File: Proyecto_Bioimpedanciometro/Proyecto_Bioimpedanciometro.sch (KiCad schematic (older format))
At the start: 29 parts, among them IC1 ATMEGA328P-A, P1 CONN_01X09, P2 CONN_01X03, P3 CONN_01X04, U1 ADG849, U2 AD8606, U3 APD3339, Y1 Crystal_Small

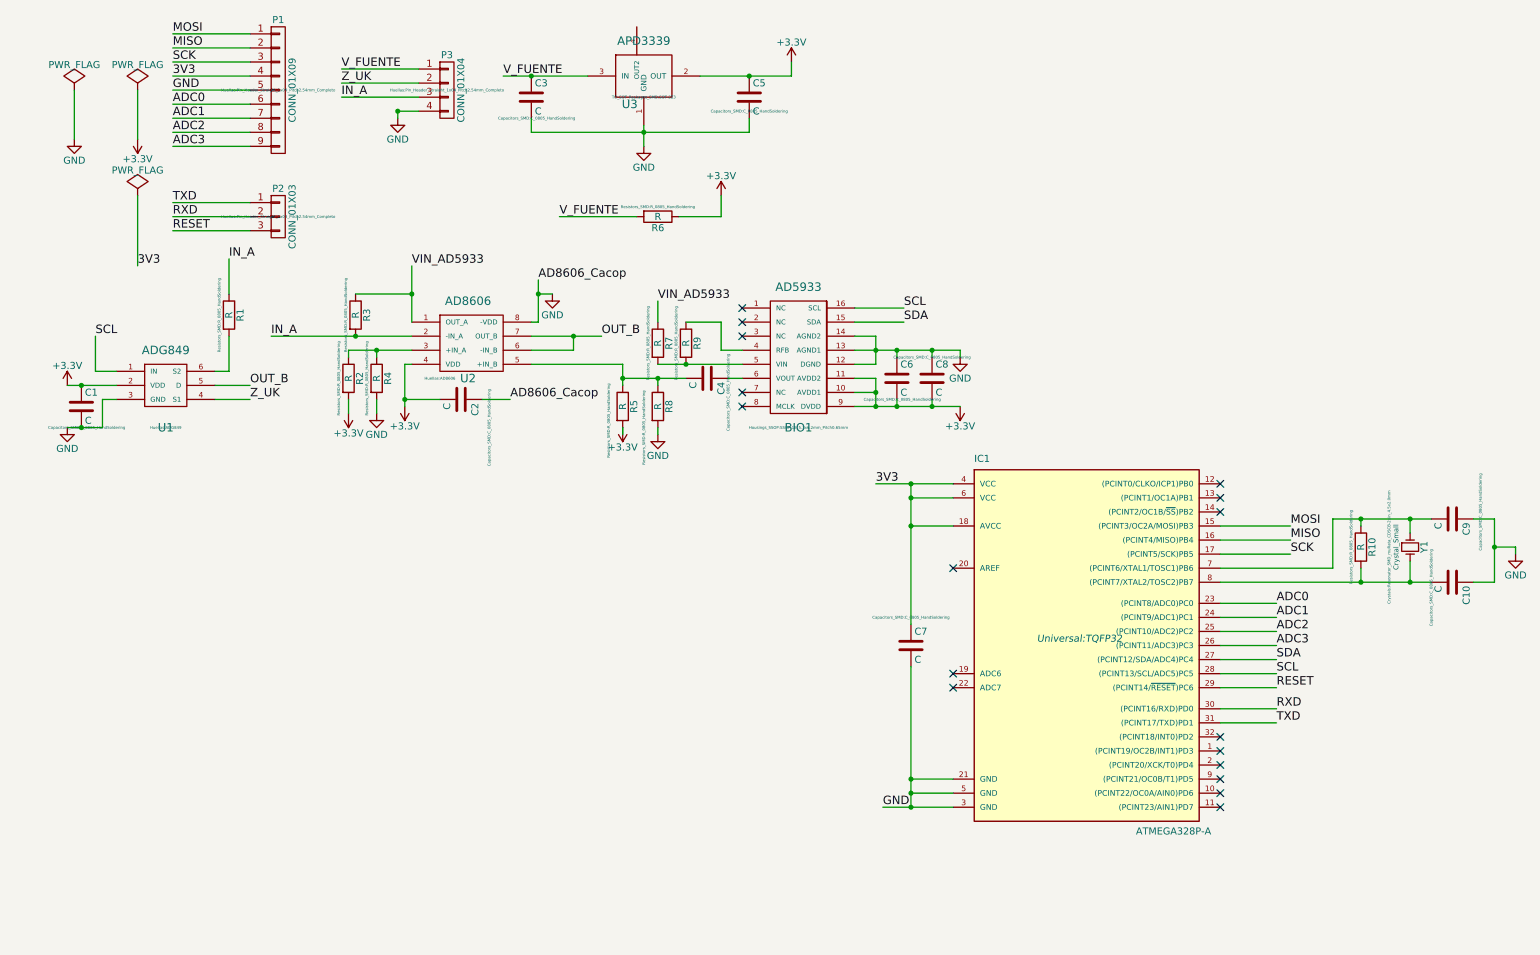
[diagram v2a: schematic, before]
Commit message: Cuarta Versión
Revisar todo el diseño y errores mas importantes
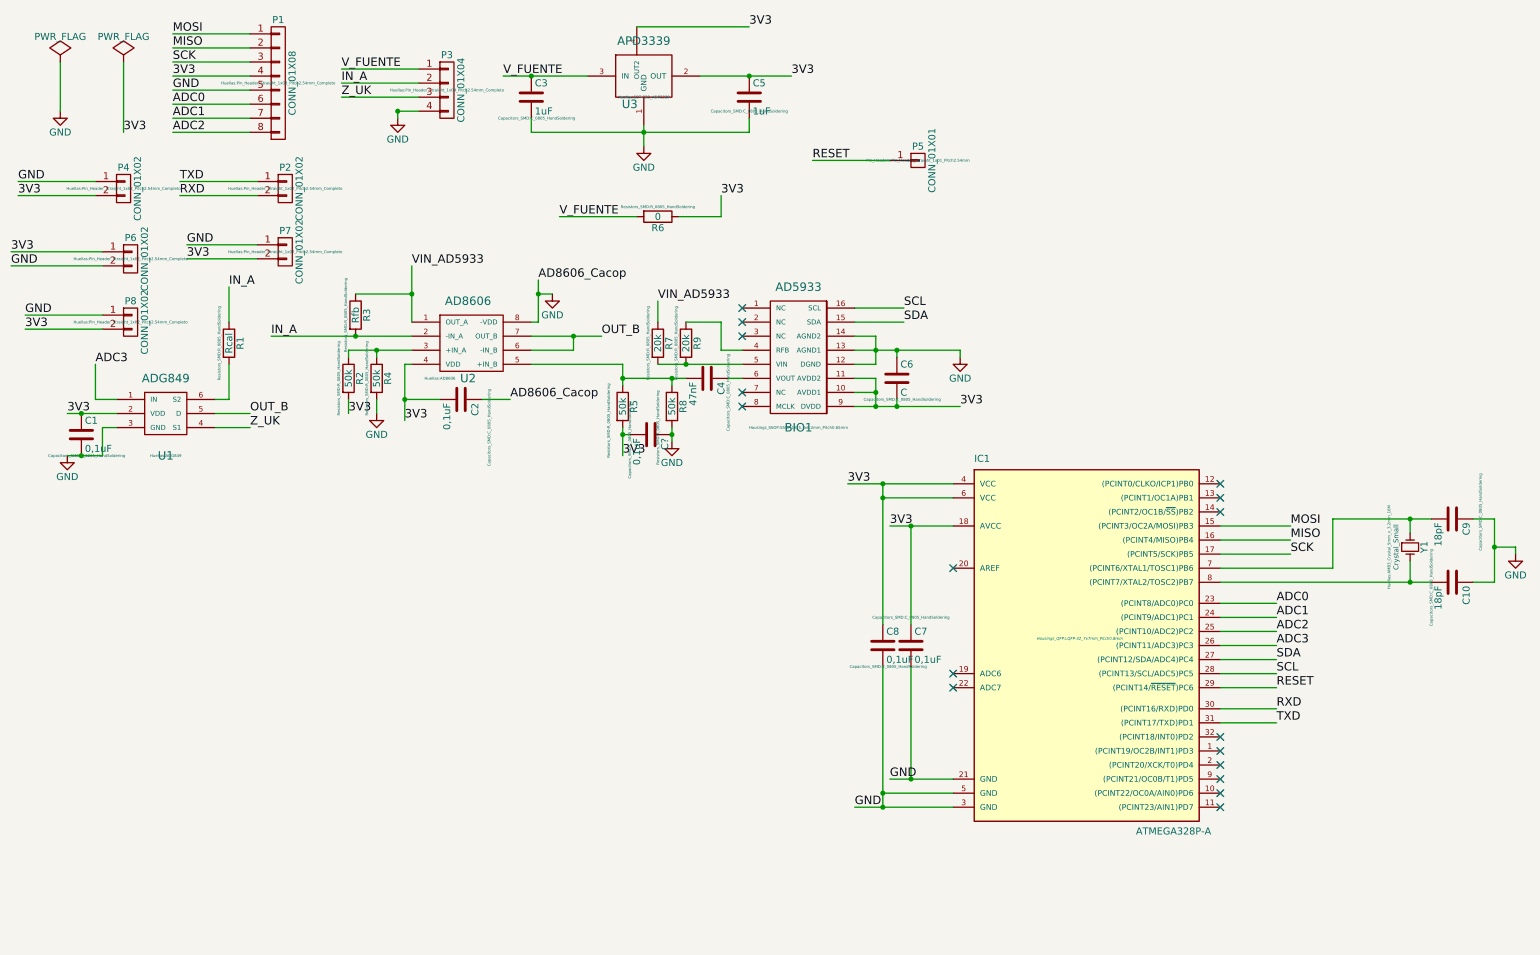
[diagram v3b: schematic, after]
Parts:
- removed P1: CONN_01X09, Huellas:Pin_Header_Straight_1x09_Pitch2.54mm_Completo, symbol CONN_01X09
- removed P2: CONN_01X03, Huellas:Pin_Header_Straight_1x03_Pitch2.54mm_Completo, symbol CONN_01X03
- removed R10: R, Resistors_SMD:R_0805_HandSoldering, symbol R
- added C?: 0,1uF, Capacitors_SMD:C_0805_HandSoldering, symbol C
- added P1: CONN_01X08, Huellas:Pin_Header_Straight_1x08_Pitch2.54mm_Completo, symbol CONN_01X08
- added P2, P4, P6, P7, P8: CONN_01X02, Huellas:Pin_Header_Straight_1x02_Pitch2.54mm_Completo, symbol CONN_01X02
- added P5: CONN_01X01, Pin_Headers:Pin_Header_Straight_1x01_Pitch2.54mm, symbol CONN_01X01
- C1, C2, C7, C8: value C -> 0,1uF
- C10, C9: value C -> 18pF
- C3, C5: value C -> 1uF
- C4: value C -> 47nF
- IC1: footprint Universal:TQFP32 -> Housings_QFP:LQFP-32_7x7mm_Pitch0.8mm
- R1: value R -> Rcal
- R2, R4, R5, R8: value R -> 50k
- R3: value R -> Rfb
- R6: value R -> 0
- R7, R9: value R -> 20k
- U3: footprint TO_SOT_Packages_SMD:SOT-223 -> Huellas:SOT-223_ADP3339
- Y1: footprint Crystals:Resonator_SMD_muRata_CDSCB-2pin_4.5x2.0mm -> Huellas:AMB3_Crystal_5mm_x_3,2mm_16M
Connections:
- net 3V3: now also BIO1.10 (AVDD1), BIO1.11 (AVDD2), BIO1.9 (DVDD), C1.1, C2.2, C5.1, C6.2, C8.1, R2.2, R5.2, R6.1, U1.2 (VDD), U2.4 (VDD), U3.2 (OUT), U3.4 (OUT2), C?.2, P1.4 (P4), P4.2 (P2), P6.1 (P1), P7.2 (P2), P8.2 (P2)
- net ADC0: now also P1.6 (P6)
- net ADC1: now also P1.7 (P7)
- net ADC2: now also P1.8 (P8)
- net ADC3: now also U1.1 (IN)
- net GND: now also C8.2, C?.1, P1.5 (P5), P4.1 (P1), P6.2 (P2), P7.1 (P1), P8.1 (P1); no longer C8.1
- net IN_A: now also P3.2 (P2); no longer P3.3 (P3)
- net MISO: now also P1.2 (P2)
- net MOSI: now also P1.1 (P1)
- net RESET: now also P5.1 (P1)
- net RXD: now also P2.2 (P2)
- net SCK: now also P1.3 (P3)
- net SCL: no longer U1.1 (IN)
- net TXD: now also P2.1 (P1)
- net Z_UK: now also P3.3 (P3); no longer P3.2 (P2)
- removed net +3V3: BIO1.10 (AVDD1), BIO1.11 (AVDD2), BIO1.9 (DVDD), C1.1, C2.2, C5.1, C6.2, C8.2, R2.2, R5.2, R6.1, U1.2 (VDD), U2.4 (VDD), U3.2 (OUT)
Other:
- moved on the sheet: C1, R1, R8, U1

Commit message: Diseño a corregir
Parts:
- gave numbers to parts that had none: 1
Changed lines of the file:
@@
 Connection ~ 5150 3100
 $Comp
-L C C?
+L C C11
 U 1 1 59133D08
 P 5000 3500
-F 0 "C?" H 5025 3600 50  0000 L CNN
+F 0 "C11" H 5025 3600 50  0000 L CNN
 F 1 "0,1uF" H 5025 3400 50  0000 L CNN
 F 2 "Capacitors_SMD:C_0805_HandSoldering" H 5038 3350 20  0000 C CNN

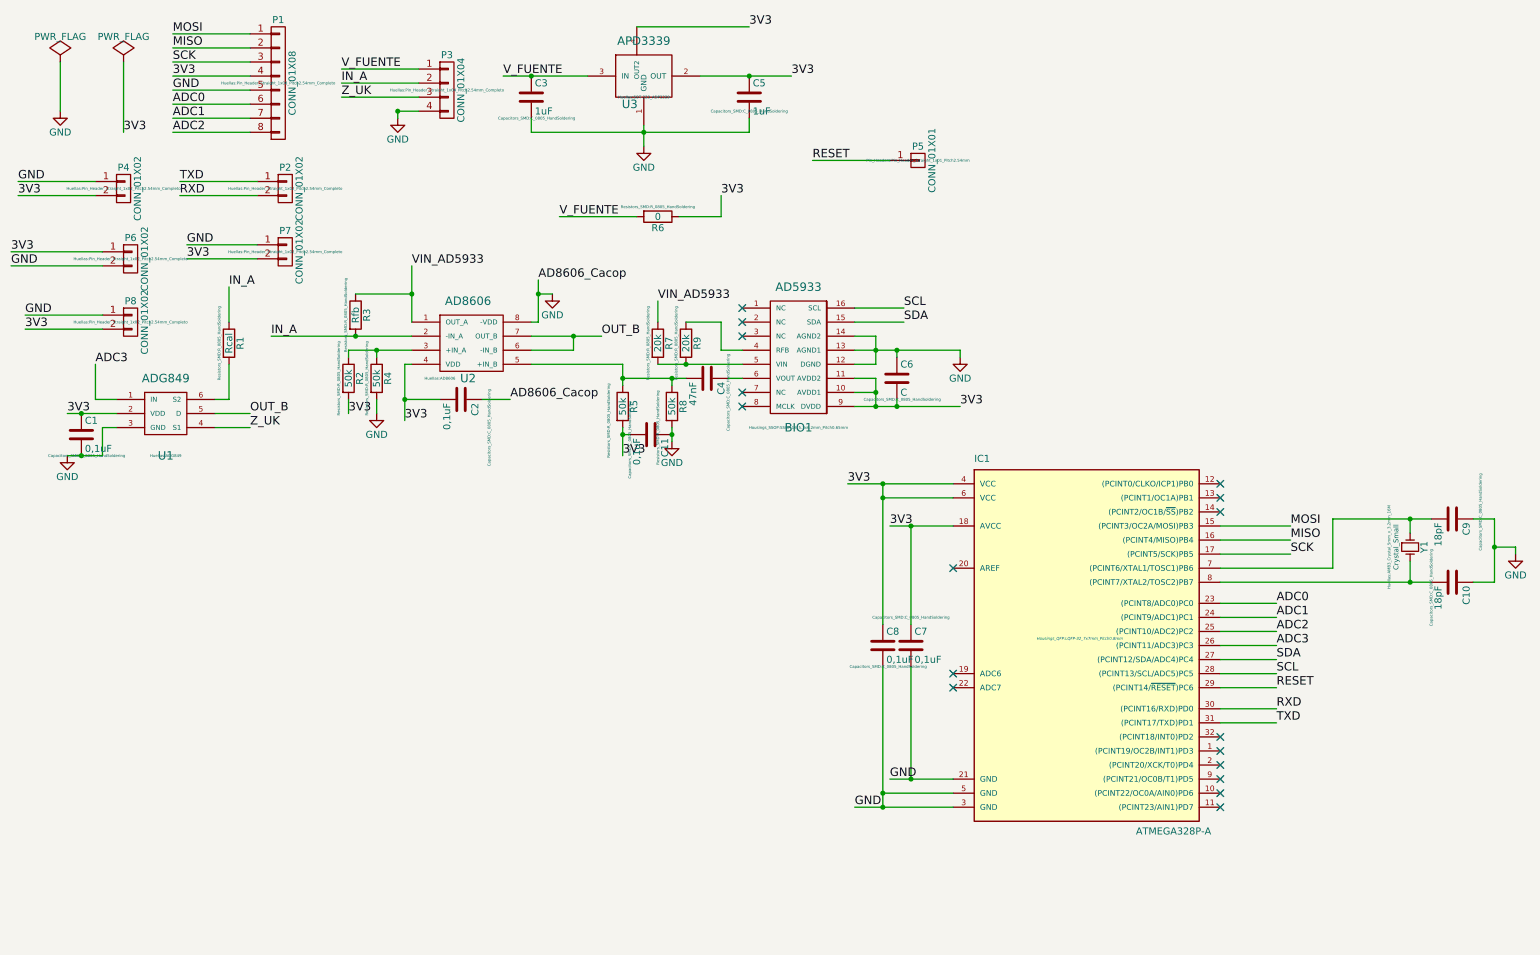
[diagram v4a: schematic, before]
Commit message: Adición del Oscilador con huella y esquematico de medidas personalizadas
Diseño sacado de otros datasheet, con valor de capacitancia recomendado
para la propia referencia
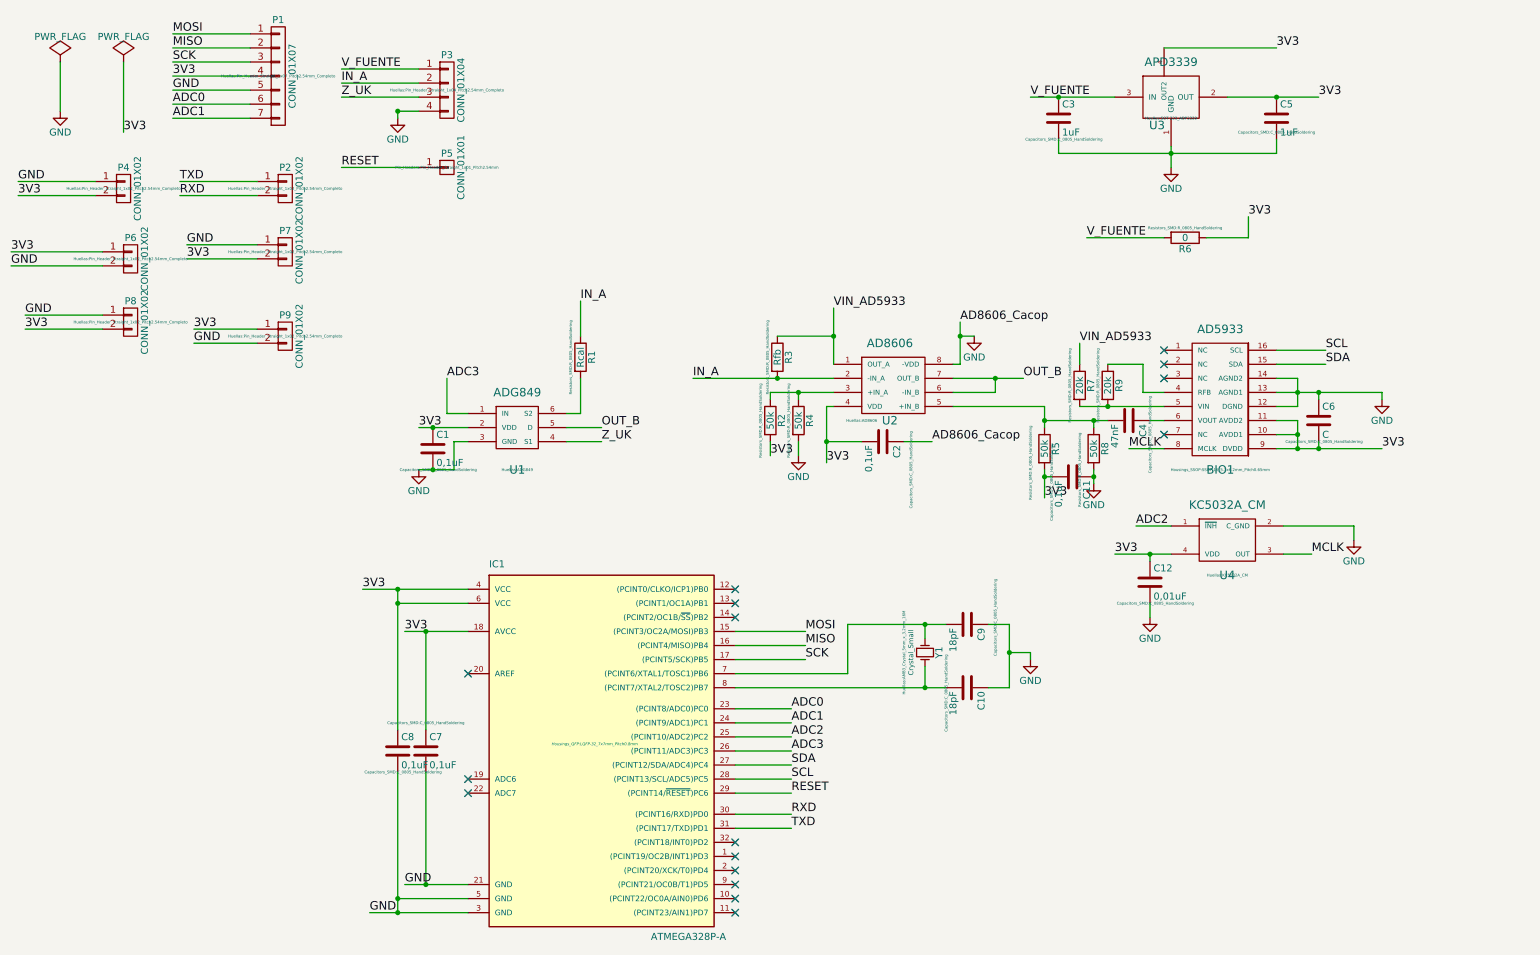
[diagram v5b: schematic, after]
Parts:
- removed P1: CONN_01X08, Huellas:Pin_Header_Straight_1x08_Pitch2.54mm_Completo, symbol CONN_01X08
- added C12: 0,01uF, Capacitors_SMD:C_0805_HandSoldering, symbol C
- added P1: CONN_01X07, Huellas:Pin_Header_Straight_1x07_Pitch2.54mm_Completo, symbol CONN_01X07
- added P9: CONN_01X02, Huellas:Pin_Header_Straight_1x02_Pitch2.54mm_Completo, symbol CONN_01X02
- added U4: KC5032A_CM, Huellas:KC5032A_CM, symbol KC5032A_CM
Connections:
- net 3V3: now also C12.1, P1.4 (P4), P9.1 (P1), U4.4 (VDD)
- net ADC0: now also P1.6 (P6)
- net ADC1: now also P1.7 (P7)
- net ADC2: now also U4.1 (~INH)
- net GND: now also C12.2, P1.5 (P5), P9.2 (P2), U4.2 (C_GND)
- net MISO: now also P1.2 (P2)
- net MOSI: now also P1.1 (P1)
- net SCK: now also P1.3 (P3)
- net MCLK: now reaches BIO1.8 (MCLK)
- net MCLK: now also U4.3 (OUT)
- no-connect marks 17 -> 16
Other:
- moved on the sheet: BIO1, C1, C10, C11, C2, C3, C4, C5, C6, C7, C8, C9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
